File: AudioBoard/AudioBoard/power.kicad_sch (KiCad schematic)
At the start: 3 parts, among them J7 Barrel_Jack, SW3 PWR_SW

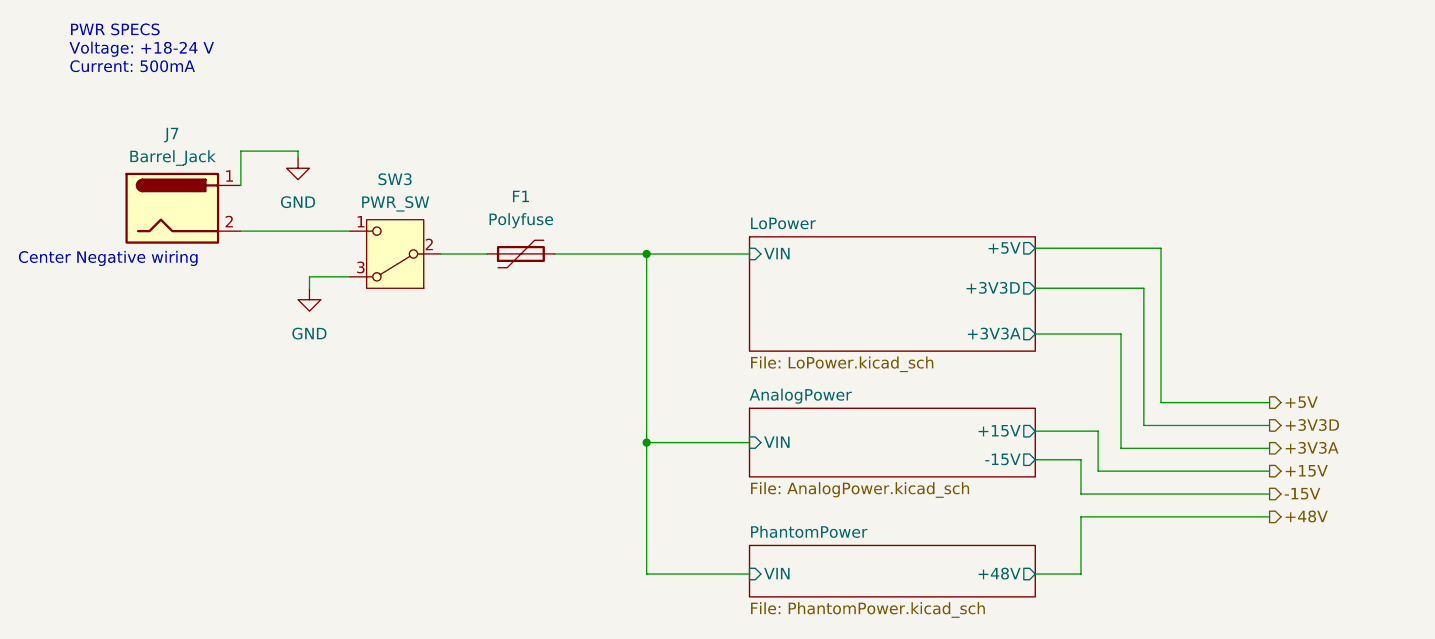
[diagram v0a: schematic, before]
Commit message: added power electronics
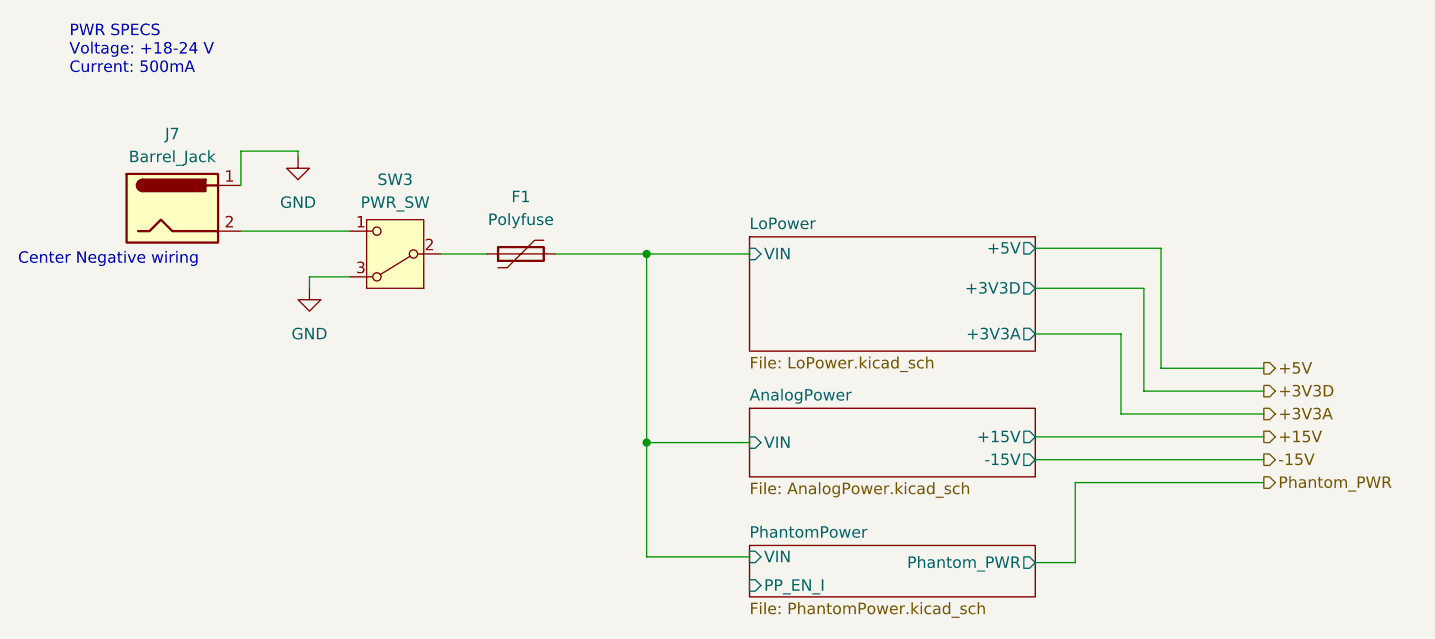
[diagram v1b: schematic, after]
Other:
- sheet PhantomPower ports: added PP_EN_I, Phantom_PWR; removed +48V
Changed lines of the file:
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@@
-	(wire
-		(pts
-			(xy 160.655 74.295) (xy 160.655 67.945)
-		)
-		(stroke
-			(width 0)
-			(type default)
-		)
-	)
 	(wire
 		(pts
@@
 	(wire
 		(pts
-			(xy 112.395 74.295) (xy 123.825 74.295)
-		)
-		(stroke
-			(width 0)
-			(type default)
-		)
-	)
-	(wire
-		(pts
-			(xy 167.64 57.785) (xy 181.61 57.785)
+			(xy 112.395 72.39) (xy 123.825 72.39)
+		)
+		(stroke
+			(width 0)
+			(type default)
+		)
+	)
+	(wire
+		(pts
+			(xy 155.575 73.025) (xy 160.02 73.025)
+		)
+		(stroke
+			(width 0)
+			(type default)
+		)
+	)
+	(wire
+		(pts
+			(xy 167.64 53.975) (xy 180.975 53.975)
+		)
+		(stroke
+			(width 0)
+			(type default)
+		)
+	)
+	(wire
+		(pts
+			(xy 160.02 73.025) (xy 160.02 64.135)
 		)
 		(stroke
@@
 	(wire
 		(pts
-			(xy 160.655 67.945) (xy 181.61 67.945)
-		)
-		(stroke
-			(width 0)
-			(type default)
-		)
-	)
-	(wire
-		(pts
-			(xy 167.64 42.545) (xy 167.64 57.785)
+			(xy 160.02 64.135) (xy 180.975 64.135)
+		)
+		(stroke
+			(width 0)
+			(type default)
+		)
+	)
+	(wire
+		(pts
+			(xy 167.64 42.545) (xy 167.64 53.975)
 		)
 		(stroke
@@
 	(wire
 		(pts
-			(xy 160.655 61.595) (xy 160.655 65.405)
-		)
-		(stroke
-			(width 0)
-			(type default)
-		)
-	)
-	(wire
-		(pts
-			(xy 181.61 55.245) (xy 169.545 55.245)
-		)
-		(stroke
-			(width 0)
-			(type default)
-		)
-	)
-	(wire
-		(pts
-			(xy 165.1 60.325) (xy 181.61 60.325)
+			(xy 180.975 51.435) (xy 169.545 51.435)
+		)
+		(stroke
+			(width 0)
+			(type default)
+		)
+	)
+	(wire
+		(pts
+			(xy 165.1 56.515) (xy 180.975 56.515)
 		)
 		(stroke
@@
 	(wire
 		(pts
-			(xy 162.56 58.42) (xy 162.56 62.865)
-		)
-		(stroke
-			(width 0)
-			(type default)
-		)
-	)
-	(wire
-		(pts
 			(xy 155.575 42.545) (xy 167.64 42.545)
 		)
@@
 	(wire
 		(pts
-			(xy 155.575 58.42) (xy 162.56 58.42)
-		)
-		(stroke
-			(width 0)
-			(type default)
-		)
-	)
-	(wire
-		(pts
-			(xy 160.655 65.405) (xy 181.61 65.405)
+			(xy 155.575 59.055) (xy 180.975 59.055)
 		)
 		(stroke
@@
 	(wire
 		(pts
-			(xy 112.395 59.69) (xy 112.395 74.295)
-		)
-		(stroke
-			(width 0)
-			(type default)
-		)
-	)
-	(wire
-		(pts
-			(xy 162.56 62.865) (xy 181.61 62.865)
-		)
-		(stroke
-			(width 0)
-			(type default)
-		)
-	)
-	(wire
-		(pts
-			(xy 155.575 74.295) (xy 160.655 74.295)
-		)
-		(stroke
-			(width 0)
-			(type default)
-		)
-	)
-	(wire
-		(pts
-			(xy 155.575 61.595) (xy 160.655 61.595)
+			(xy 112.395 59.69) (xy 112.395 72.39)
+		)
+		(stroke
+			(width 0)
+			(type default)
+		)
+	)
+	(wire
+		(pts
+			(xy 155.575 61.595) (xy 180.975 61.595)
 		)
 		(stroke
@@
 	(wire
 		(pts
-			(xy 169.545 55.245) (xy 169.545 38.1)
-		)
-		(stroke
-			(width 0)
-			(type default)
-		)
-	)
-	(wire
-		(pts
-			(xy 165.1 47.625) (xy 165.1 60.325)
+			(xy 169.545 51.435) (xy 169.545 38.1)
+		)
+		(stroke
+			(width 0)
+			(type default)
+		)
+	)
+	(wire
+		(pts
+			(xy 165.1 47.625) (xy 165.1 56.515)
 		)
 		(stroke
@@
 	(hierarchical_label "+3V3A"
 		(shape output)
-		(at 181.61 60.325 0)
+		(at 180.975 56.515 0)
 		(effects
 			(font
@@
 	(hierarchical_label "+3V3D"
 		(shape output)
-		(at 181.61 57.785 0)
+		(at 180.975 53.975 0)
 		(effects
 			(font
@@
 	(hierarchical_label "+5V"
 		(shape output)
-		(at 181.61 55.245 0)
+		(at 180.975 51.435 0)
 		(effects
 			(font
@@
 		)
 	)
-	(hierarchical_label "+48V"
+	(hierarchical_label "Phantom_PWR"
 		(shape output)
-		(at 181.61 67.945 0)
+		(at 180.975 64.135 0)
 		(effects
 			(font
@@
 	(hierarchical_label "-15V"
 		(shape output)
-		(at 181.61 65.405 0)
+		(at 180.975 61.595 0)
 		(effects
 			(font
@@
 	(hierarchical_label "+15V"
 		(shape output)
-		(at 181.61 62.865 0)
+		(at 180.975 59.055 0)
 		(effects
 			(font
@@
 			)
 		)
-		(pin "+48V" output
-			(at 155.575 74.295 0)
+		(pin "VIN" input
+			(at 123.825 72.39 180)
+			(effects
+				(font
+					(size 1.27 1.27)
+				)
+				(justify left)
+			)
+		)
+		(pin "PP_EN_I" input
+			(at 123.825 75.565 180)
+			(effects
+				(font
+					(size 1.27 1.27)
+				)
+				(justify left)
+			)
+		)
+		(pin "Phantom_PWR" output
+			(at 155.575 73.025 0)
 			(effects
 				(font
@@
 				)
 				(justify right)
-			)
-		)
-		(pin "VIN" input
-			(at 123.825 74.295 180)
-			(effects
-				(font
-					(size 1.27 1.27)
-				)
-				(justify left)
 			)
 		)
@@
 		)
 		(pin "+15V" output
-			(at 155.575 58.42 0)
-			(effects
-				(font
+			(at 155.575 59.055 0)
+			(effects
+				(font
